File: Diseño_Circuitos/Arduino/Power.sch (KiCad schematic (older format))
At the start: 20 parts

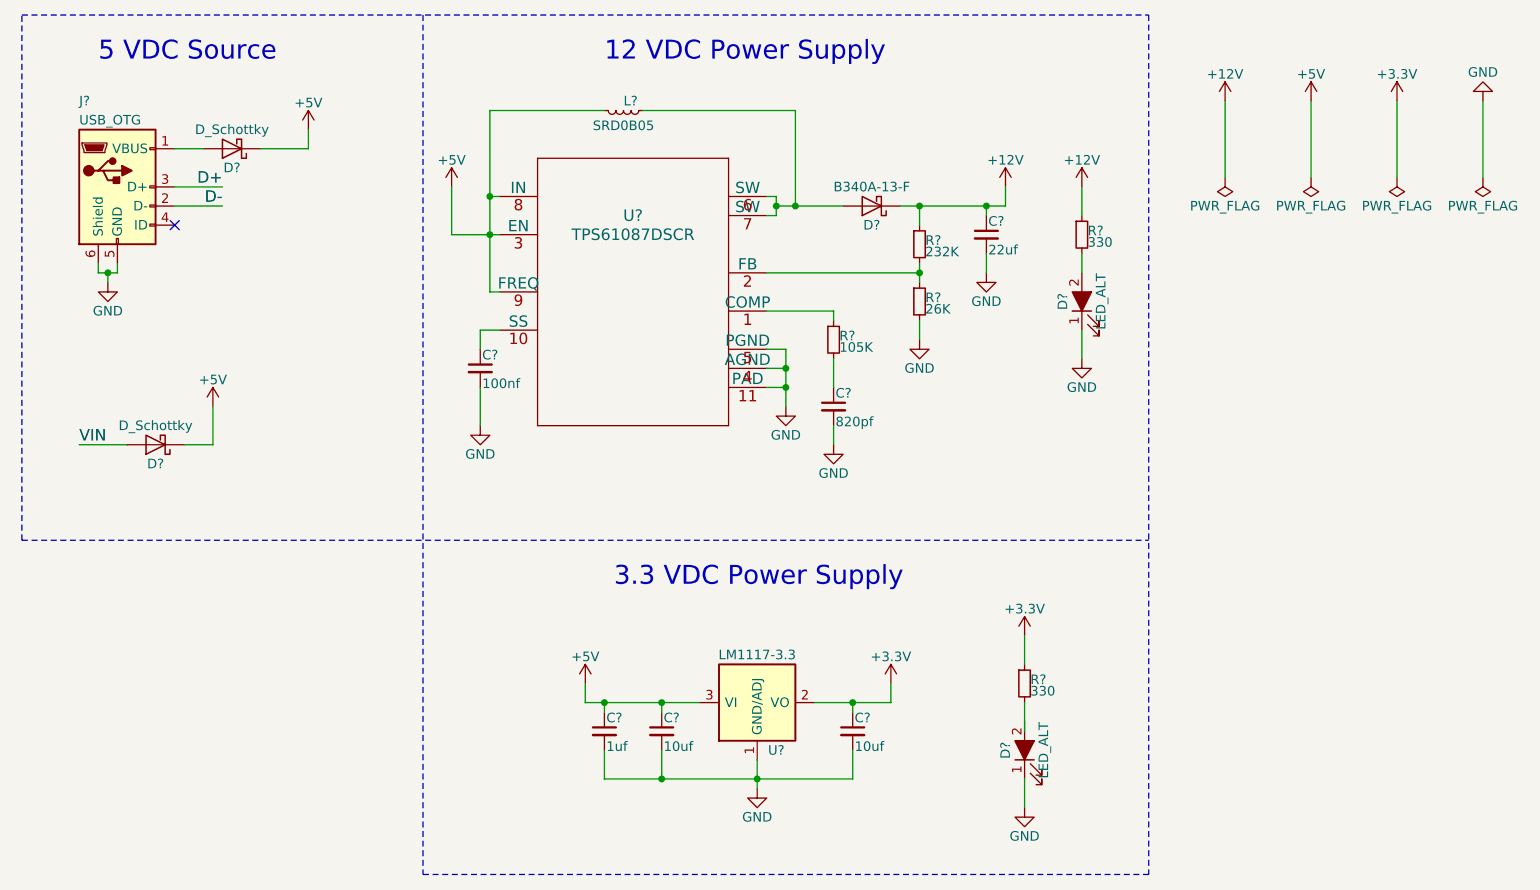
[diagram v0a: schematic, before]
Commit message: schematic completed
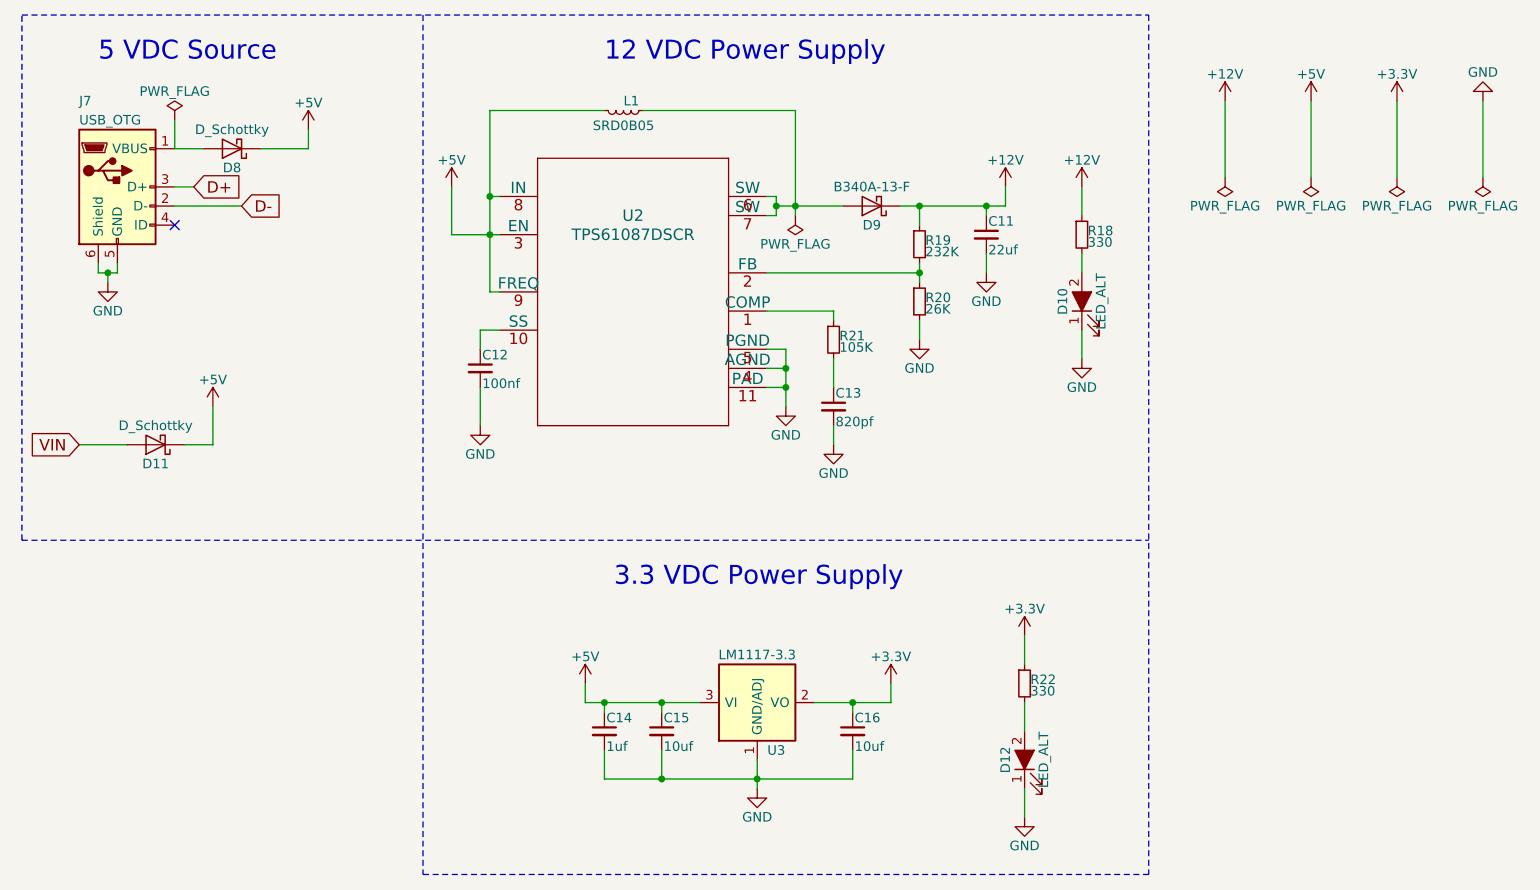
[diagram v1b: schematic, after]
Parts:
- gave numbers to parts that had none: 20
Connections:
- net at D12.2 (A): now also R22.2
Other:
- moved on the sheet: D12

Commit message: pcb components placed
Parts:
- removed D11, D8: D_Schottky, symbol D_Schottky
- removed D9: B340A-13-F, symbol D_Schottky
- added D11, D8, D9: B340A-13-F, custom footprints:DIOM5226X240N, symbol B340A-13-F
- C11, C12, C13, C14, C15, C16: footprint (none) -> custom footprints:C_0805_HandSoldering
- D10, D12: footprint (none) -> custom footprints:LED_0805
- J7: footprint (none) -> custom footprints:47346-0001
- L1: footprint (none) -> custom footprints:SDR0805-332KL
- R18, R19, R20, R21, R22: footprint (none) -> custom footprints:R_0805_HandSoldering
- U2: footprint DSC0010A -> custom footprints:TPS61087DSCR
- U3: footprint (none) -> custom footprints:TO-252-2
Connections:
- net +12V: now also D9.C
- net +5V: now also D11.C, D8.C
- net VIN: now also D11.A
- net at L1.1, U2.6 (SW), U2.7 (SW): now also D9.A
- net at J7.1 (VBUS): now also D8.A
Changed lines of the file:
@@
 F 0 "U2" H 3800 2450 60  0000 C CNN
 F 1 "TPS61087DSCR" H 3800 2350 60  0000 C CNN
-F 2 "DSC0010A" H 3800 2290 60  0001 C CNN
+F 2 "custom footprints:TPS61087DSCR" H 3800 2290 60  0001 C CNN
 F 3 "" H 3800 2350 60  0000 C CNN
 	1    3800 2050
 	1    0    0    -1
-$EndComp
-$Comp
-L D_Schottky D9
-U 1 1 5F73A16B
-P 5050 1600
-F 0 "D9" H 5050 1700 50  0000 C CNN
-F 1 "B340A-13-F" H 5050 1500 50  0000 C CNN
-F 2 "" H 5050 1600 50  0000 C CNN
-F 3 "" H 5050 1600 50  0000 C CNN
-	1    5050 1600
-	-1   0    0    1
 $EndComp
 $Comp
@@
 F 0 "U3" H 4550 3950 50  0000 C CNN
 F 1 "LM1117-3.3" H 4450 4450 50  0000 C CNN
-F 2 "" H 4450 4200 50  0000 C CNN
+F 2 "custom footprints:TO-252-2" H 4450 4200 50  0001 C CNN
 F 3 "" H 4450 4200 50  0000 C CNN
 	1    4450 4200
@@
 F 0 "C15" H 3960 4420 50  0000 L CNN
 F 1 "10uf" H 3960 4270 50  0000 L CNN
-F 2 "" H 3950 4350 50  0000 C CNN
+F 2 "custom footprints:C_0805_HandSoldering" H 3950 4350 50  0001 C CNN
 F 3 "" H 3950 4350 50  0000 C CNN
 	1    3950 4350
@@
 F 0 "R21" H 4880 2320 50  0000 L CNN
 F 1 "105K" H 4880 2260 50  0000 L CNN
-F 2 "" H 4850 2300 50  0000 C CNN
+F 2 "custom footprints:R_0805_HandSoldering" H 4850 2300 50  0001 C CNN
 F 3 "" H 4850 2300 50  0000 C CNN
 	1    4850 2300
@@
 F 0 "L1" V 3700 1100 50  0000 L CNN
 F 1 "SRD0B05" V 3800 1100 50  0000 C TNN
-F 2 "" H 3750 1100 50  0000 C CNN
+F 2 "custom footprints:SDR0805-332KL" H 3750 1100 50  0001 C CNN
 F 3 "" H 3750 1100 50  0000 C CNN
 	1    3750 1100
@@
 F 0 "C12" H 3010 2520 50  0000 L CNN
 F 1 "100nf" H 3010 2370 50  0000 L CNN
-F 2 "" H 3000 2450 50  0000 C CNN
+F 2 "custom footprints:C_0805_HandSoldering" H 3000 2450 50  0001 C CNN
 F 3 "" H 3000 2450 50  0000 C CNN
 	1    3000 2450
@@
 F 0 "C11" H 5660 1820 50  0000 L CNN
 F 1 "22uf" H 5660 1670 50  0000 L CNN
-F 2 "" H 5650 1750 50  0000 C CNN
+F 2 "custom footprints:C_0805_HandSoldering" H 5650 1750 50  0001 C CNN
 F 3 "" H 5650 1750 50  0000 C CNN
 	1    5650 1750
@@
 F 0 "C13" H 4860 2720 50  0000 L CNN
 F 1 "820pf" H 4860 2570 50  0000 L CNN
-F 2 "" H 4850 2650 50  0000 C CNN
+F 2 "custom footprints:C_0805_HandSoldering" H 4850 2650 50  0001 C CNN
 F 3 "" H 4850 2650 50  0000 C CNN
 	1    4850 2650
@@
 F 0 "C14" H 3660 4420 50  0000 L CNN
 F 1 "1uf" H 3660 4270 50  0000 L CNN
-F 2 "" H 3650 4350 50  0000 C CNN
+F 2 "custom footprints:C_0805_HandSoldering" H 3650 4350 50  0001 C CNN
 F 3 "" H 3650 4350 50  0000 C CNN
 	1    3650 4350
@@
 F 0 "C16" H 4960 4420 50  0000 L CNN
 F 1 "10uf" H 4960 4270 50  0000 L CNN
-F 2 "" H 4950 4350 50  0000 C CNN
+F 2 "custom footprints:C_0805_HandSoldering" H 4950 4350 50  0001 C CNN
 F 3 "" H 4950 4350 50  0000 C CNN
 	1    4950 4350
@@
 F 0 "R20" H 5330 2120 50  0000 L CNN
 F 1 "26K" H 5330 2060 50  0000 L CNN
-F 2 "" H 5300 2100 50  0000 C CNN
+F 2 "custom footprints:R_0805_HandSoldering" H 5300 2100 50  0001 C CNN
 F 3 "" H 5300 2100 50  0000 C CNN
 	1    5300 2100
@@
 F 0 "R19" H 5330 1820 50  0000 L CNN
 F 1 "232K" H 5330 1760 50  0000 L CNN
-F 2 "" H 5300 1800 50  0000 C CNN
+F 2 "custom footprints:R_0805_HandSoldering" H 5300 1800 50  0001 C CNN
 F 3 "" H 5300 1800 50  0000 C CNN
 	1    5300 1800
@@
 F 0 "J7" H 900 1950 50  0000 L CNN
 F 1 "USB_OTG" H 900 1850 50  0000 L CNN
-F 2 "" H 1250 1450 50  0001 C CNN
+F 2 "custom footprints:47346-0001" H 1250 1450 50  0001 C CNN
 F 3 "" H 1250 1450 50  0001 C CNN
 	1    1100 1500
@@
 L +5V #PWR046
 U 1 1 5F73A419
-P 2100 1200
-F 0 "#PWR046" H 2100 1050 50  0001 C CNN
-F 1 "+5V" H 2100 1340 50  0000 C CNN
-F 2 "" H 2100 1200 50  0001 C CNN
-F 3 "" H 2100 1200 50  0001 C CNN
-	1    2100 1200
+P 2200 1200
+F 0 "#PWR046" H 2200 1050 50  0001 C CNN
+F 1 "+5V" H 2200 1340 50  0000 C CNN
+F 2 "" H 2200 1200 50  0001 C CNN
+F 3 "" H 2200 1200 50  0001 C CNN
+	1    2200 1200
 	1    0    0    -1
 $EndComp
@@
 $EndComp
 $Comp
-L D_Schottky D8
-U 1 1 5F73AEE1
-P 1700 1300
-F 0 "D8" H 1700 1400 50  0000 C CNN
-F 1 "D_Schottky" H 1700 1200 50  0000 C CNN
-F 2 "" H 1700 1300 50  0000 C CNN
-F 3 "" H 1700 1300 50  0000 C CNN
-	1    1700 1300
-	-1   0    0    1
-$EndComp
-$Comp
 L +5V #PWR056
 U 1 1 5F73B4E3
-P 1600 2650
-F 0 "#PWR056" H 1600 2500 50  0001 C CNN
-F 1 "+5V" H 1600 2790 50  0000 C CNN
-F 2 "" H 1600 2650 50  0001 C CNN
-F 3 "" H 1600 2650 50  0001 C CNN
-	1    1600 2650
-	1    0    0    -1
-$EndComp
-$Comp
-L D_Schottky D11
-U 1 1 5F73B5EF
-P 1300 2850
-F 0 "D11" H 1300 2950 50  0000 C CNN
-F 1 "D_Schottky" H 1300 2750 50  0000 C CNN
-F 2 "" H 1300 2850 50  0000 C CNN
-F 3 "" H 1300 2850 50  0000 C CNN
-	1    1300 2850
-	-1   0    0    1
+P 1700 2650
+F 0 "#PWR056" H 1700 2500 50  0001 C CNN
+F 1 "+5V" H 1700 2790 50  0000 C CNN
+F 2 "" H 1700 2650 50  0001 C CNN
+F 3 "" H 1700 2650 50  0001 C CNN
+	1    1700 2650
+	1    0    0    -1
 $EndComp
 $Comp
@@
 F 0 "D12" H 5850 4600 50  0000 C CNN
 F 1 "LED_ALT" H 5850 4400 50  0000 C CNN
-F 2 "" H 5850 4500 50  0000 C CNN
+F 2 "custom footprints:LED_0805" H 5850 4500 50  0001 C CNN
 F 3 "" H 5850 4500 50  0000 C CNN
 	1    5850 4500
@@
 F 0 "R22" H 5880 4120 50  0000 L CNN
 F 1 "330" H 5880 4060 50  0000 L CNN
-F 2 "" H 5850 4100 50  0000 C CNN
+F 2 "custom footprints:R_0805_HandSoldering" H 5850 4100 50  0001 C CNN
 F 3 "" H 5850 4100 50  0000 C CNN
 	1    5850 4100
@@
 F 0 "D10" H 6150 2200 50  0000 C CNN
 F 1 "LED_ALT" H 6150 2000 50  0000 C CNN
-F 2 "" H 6150 2100 50  0000 C CNN
+F 2 "custom footprints:LED_0805" H 6150 2100 50  0001 C CNN
 F 3 "" H 6150 2100 50  0000 C CNN
 	1    6150 2100
@@
 F 0 "R18" H 6180 1770 50  0000 L CNN
 F 1 "330" H 6180 1710 50  0000 L CNN
-F 2 "" H 6150 1750 50  0000 C CNN
+F 2 "custom footprints:R_0805_HandSoldering" H 6150 1750 50  0001 C CNN
 F 3 "" H 6150 1750 50  0000 C CNN
 	1    6150 1750
@@
 Wire Wire Line
 	4550 1550 4500 1550
-Wire Wire Line
-	4550 1600 4900 1600
 Connection ~ 4550 1600
 Wire Wire Line
@@
 	1400 1300 1550 1300
 Wire Wire Line
-	1850 1300 2100 1300
-Wire Wire Line
-	2100 1300 2100 1200
+	1950 1300 2200 1300
+Wire Wire Line
+	2200 1300 2200 1200
 Wire Wire Line
 	900  2850 1150 2850
 Wire Wire Line
-	1450 2850 1600 2850
-Wire Wire Line
-	1600 2850 1600 2650
+	1550 2850 1700 2850
+Wire Wire Line
+	1700 2850 1700 2650
 Wire Wire Line
 	6150 1500 6150 1650
@@
 Wire Wire Line
 	1400 1150 1400 1300
+$Comp
+L B340A-13-F D9
+U 1 1 5F79276D
+P 5000 1600
+F 0 "D9" H 4800 1700 50  0000 L BNN
+F 1 "B340A-13-F" H 4800 1450 50  0000 L BNN
+F 2 "custom footprints:DIOM5226X240N" H 4950 1800 50  0001 L BNN
+F 3 "" H 5100 1750 50  0001 L BNN
+F 4 "17-2" H 5000 1600 50  0001 L BNN "Campo4"
+	1    5000 1600
+	1    0    0    -1
+$EndComp
+Wire Wire Line
+	4800 1600 4550 1600
+$Comp
+L B340A-13-F D8
+U 1 1 5F792D17
+P 1750 1300
+F 0 "D8" H 1550 1400 50  0000 L BNN
+F 1 "B340A-13-F" H 1550 1150 50  0000 L BNN
+F 2 "custom footprints:DIOM5226X240N" H 1700 1500 50  0001 L BNN
+F 3 "" H 1850 1450 50  0001 L BNN
+F 4 "17-2" H 1750 1300 50  0001 L BNN "Campo4"
+	1    1750 1300
+	1    0    0    -1
+$EndComp
+$Comp
+L B340A-13-F D11
+U 1 1 5F792D85
+P 1350 2850
+F 0 "D11" H 1150 2950 50  0000 L BNN
+F 1 "B340A-13-F" H 1150 2700 50  0000 L BNN
+F 2 "custom footprints:DIOM5226X240N" H 1300 3050 50  0001 L BNN
+F 3 "" H 1450 3000 50  0001 L BNN
+F 4 "17-2" H 1350 2850 50  0001 L BNN "Campo4"
+	1    1350 2850
+	1    0    0    -1
+$EndComp
 $EndSCHEMATC
